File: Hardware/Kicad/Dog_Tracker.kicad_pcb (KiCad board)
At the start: 4 copper layers, 109 x 53.7 mm, 22 parts, among them IC1 M4 Feather, U1 ADP160AUJZ-1.8-R7, U2 SX1280IMLTRT, U3 Origin_GPS1510, U5 SN74AUP1T97, U6 LSM6DSO32

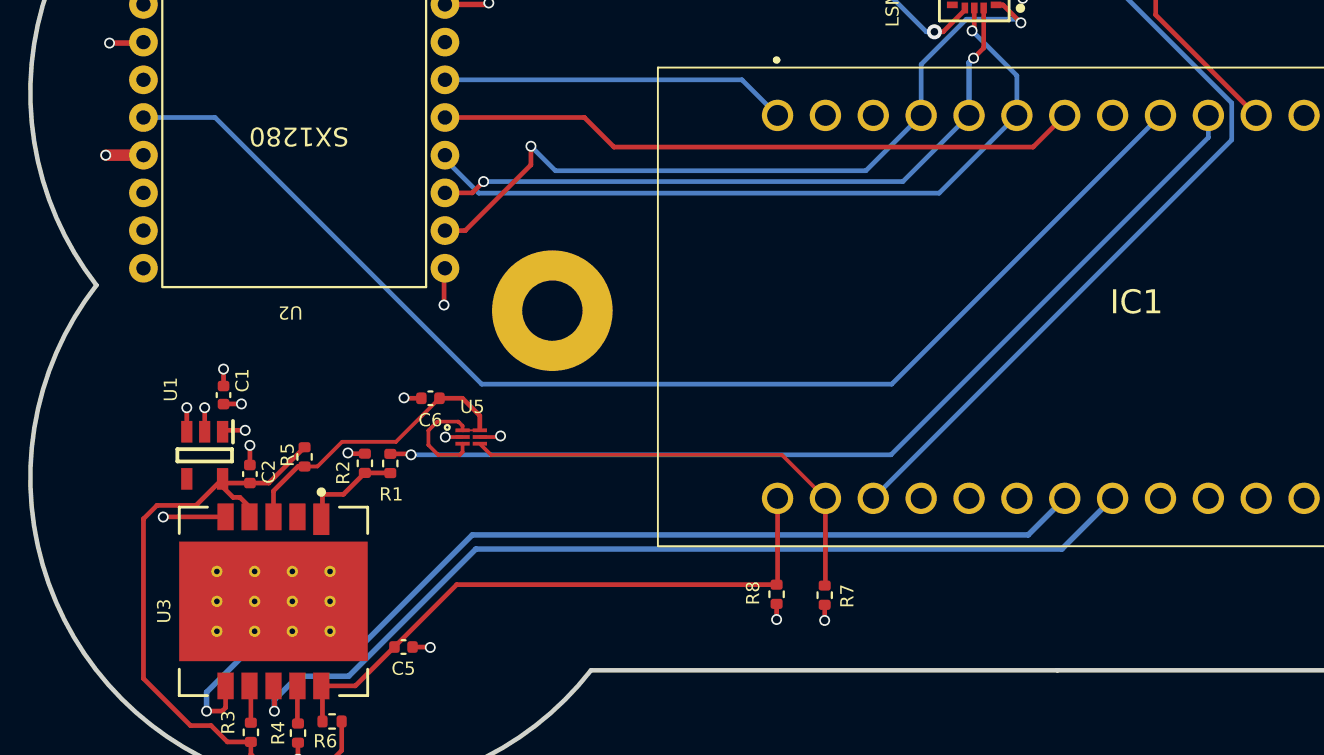
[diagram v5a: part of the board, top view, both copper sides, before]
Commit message: 'update pcb based on steves comments'
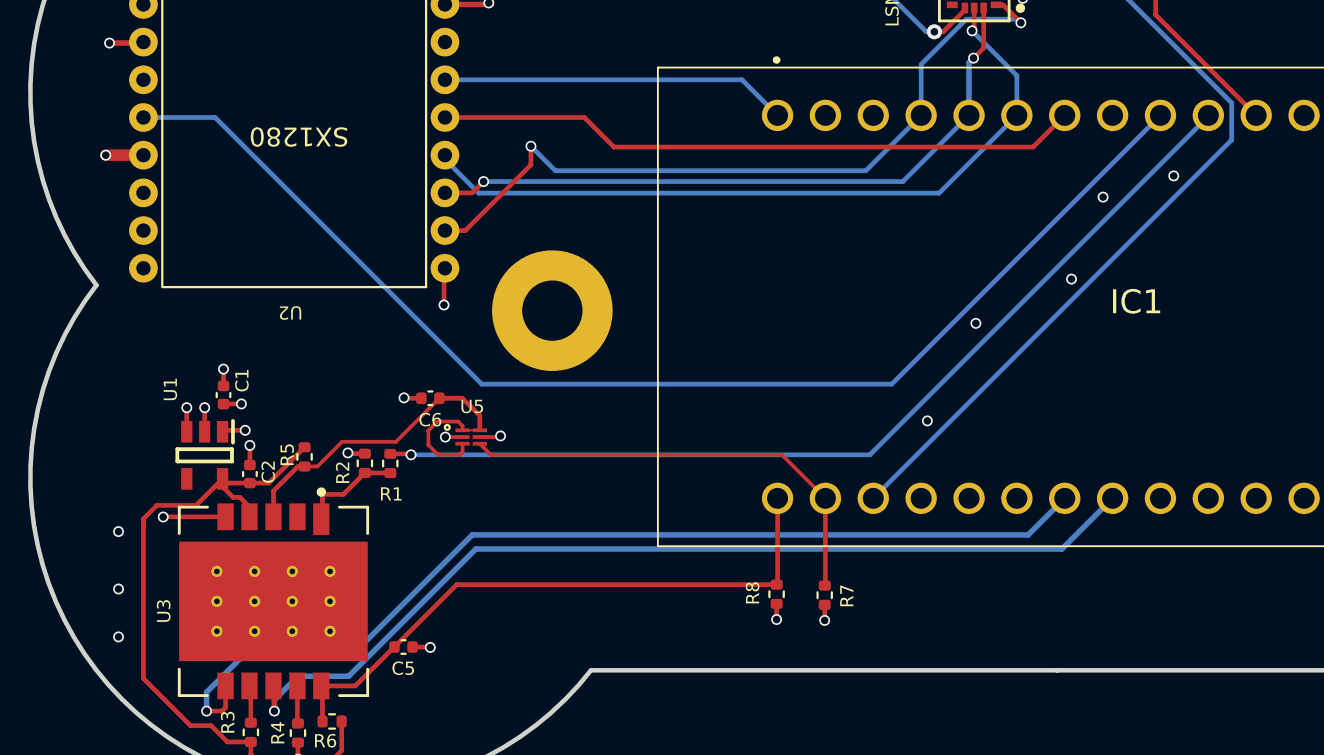
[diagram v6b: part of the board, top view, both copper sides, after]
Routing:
- net /GPS_ON: track 51.6 -> 50.9 mm
- net GND: vias 23 -> 31
- added copper zone on B.Cu, net GND
- added copper zone on F.Cu, net GND
- removed copper zone on F.Cu, net (none)
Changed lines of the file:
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@@
       (outputformat 1)
       (mirror false)
-      (drillshape 1)
+      (drillshape 0)
       (scaleselection 1)
-      (outputdirectory "")
+      (outputdirectory "./")
     )
   )
@@
   (segment (start 65.8 87.85) (end 63.55 87.85) (width 0.29337) (layer "F.Cu") (net 2))
   (via (at 58.4 111.65) (size 0.58) (drill 0.4) (layers "F.Cu" "B.Cu") (free) (net 2))
+  (via (at 96.8 102.425) (size 0.58) (drill 0.4) (layers "F.Cu" "B.Cu") (free) (net 2))
   (via (at 64.83 80.82) (size 0.8) (drill 0.4) (layers "F.Cu" "B.Cu") (net 2))
   (via (at 63.57 110.81) (size 0.58) (drill 0.4) (layers "F.Cu" "B.Cu") (net 2))
@@
   (via (at 94.2125 85.875) (size 0.58) (drill 0.4) (layers "F.Cu" "B.Cu") (free) (net 2))
   (via (at 45.75 89.9) (size 0.58) (drill 0.4) (layers "F.Cu" "B.Cu") (free) (net 2))
+  (via (at 98.475 98.075) (size 0.58) (drill 0.4) (layers "F.Cu" "B.Cu") (free) (net 2))
   (via (at 65.877798 87.772202) (size 0.58) (drill 0.4) (layers "F.Cu" "B.Cu") (free) (net 2))
   (via (at 64.83 78.82) (size 0.8) (drill 0.4) (layers "F.Cu" "B.Cu") (net 2))
   (via (at 51.8 107.2) (size 0.58) (drill 0.4) (layers "F.Cu" "B.Cu") (free) (net 2))
   (via (at 55.75 127.9) (size 0.58) (drill 0.4) (layers "F.Cu" "B.Cu") (free) (net 2))
+  (via (at 102.225 96.95) (size 0.58) (drill 0.4) (layers "F.Cu" "B.Cu") (free) (net 2))
+  (via (at 46.228 118.872) (size 0.58) (drill 0.4) (layers "F.Cu" "B.Cu") (free) (net 2))
   (via (at 91.3125 83.575) (size 0.58) (drill 0.4) (layers "F.Cu" "B.Cu") (free) (net 2))
   (via (at 48.6 115.05) (size 0.58) (drill 0.4) (layers "F.Cu" "B.Cu") (free) (net 2))
   (via (at 50.8 78.92) (size 0.8) (drill 0.4) (layers "F.Cu" "B.Cu") (net 2))
+  (via (at 89.15 109.95) (size 0.58) (drill 0.4) (layers "F.Cu" "B.Cu") (free) (net 2))
   (via (at 91.11 85.02) (size 0.58) (drill 0.4) (layers "F.Cu" "B.Cu") (free) (net 2))
   (via (at 53.2 111.25) (size 0.58) (drill 0.4) (layers "F.Cu" "B.Cu") (free) (net 2))
   (via (at 64.83 79.82) (size 0.8) (drill 0.4) (layers "F.Cu" "B.Cu") (net 2))
   (via (at 94.2125 87.525) (size 0.58) (drill 0.4) (layers "F.Cu" "B.Cu") (free) (net 2))
+  (via (at 46.228 121.412) (size 0.58) (drill 0.4) (layers "F.Cu" "B.Cu") (free) (net 2))
   (via (at 63.5 103.8) (size 0.58) (drill 0.4) (layers "F.Cu" "B.Cu") (free) (net 2))
+  (via (at 46.228 115.824) (size 0.58) (drill 0.4) (layers "F.Cu" "B.Cu") (free) (net 2))
   (via (at 89.2125 86.875) (size 0.58) (drill 0.4) (layers "F.Cu" "B.Cu") (free) (net 2))
   (via (at 50.8 109.25) (size 0.58) (drill 0.4) (layers "F.Cu" "B.Cu") (free) (net 2))
   (via (at 62.7715 121.973) (size 0.58) (drill 0.4) (layers "F.Cu" "B.Cu") (free) (net 2))
   (via (at 94.2125 86.725) (size 0.58) (drill 0.4) (layers "F.Cu" "B.Cu") (free) (net 2))
+  (via (at 91.725 104.775) (size 0.58) (drill 0.4) (layers "F.Cu" "B.Cu") (free) (net 2))
   (segment (start 52.007 126.987) (end 53.249999 126.987) (width 0.25) (layer "F.Cu") (net 3))
   (segment (start 56.99 128.52) (end 54.13 128.52) (width 0.25) (layer "F.Cu") (net 3))
@@
   (segment (start 61.7 111.7) (end 61.75 111.75) (width 0.25) (layer "F.Cu") (net 13))
   (via (at 61.75 111.75) (size 0.58) (drill 0.4) (layers "F.Cu" "B.Cu") (net 13))
-  (segment (start 61.75 111.75) (end 87.22 111.75) (width 0.25) (layer "B.Cu") (net 13))
-  (segment (start 87.22 111.75) (end 104.06 94.91) (width 0.25) (layer "B.Cu") (net 13))
-  (segment (start 104.06 94.91) (end 104.06 93.74) (width 0.25) (layer "B.Cu") (net 13))
+  (segment (start 104.06 93.79) (end 104.06 93.74) (width 0.25) (layer "B.Cu") (net 13))
+  (segment (start 61.75 111.75) (end 86.1 111.75) (width 0.25) (layer "B.Cu") (net 13))
+  (segment (start 86.1 111.75) (end 104.06 93.79) (width 0.25) (layer "B.Cu") (net 13))
   (segment (start 101.266 85.558) (end 101.266 88.406) (width 0.25) (layer "F.Cu") (net 14))
   (segment (start 101.266 88.406) (end 106.6 93.74) (width 0.25) (layer "F.Cu") (net 14))
@@
   (segment (start 55.719999 125.977) (end 55.749999 126.007) (width 0.25) (layer "F.Cu") (net 43))
   (segment (start 55.719999 124.012) (end 55.719999 125.977) (width 0.25) (layer "F.Cu") (net 43))
-  (zone (net 0) (net_name "") (layer "F.Cu") (hatch edge 0.508)
+  (zone (net 2) (net_name "GND") (layer "F.Cu") (hatch edge 0.508)
     (connect_pads (clearance 0))
     (min_thickness 0.254) (filled_areas_thickness no)
@@
     (polygon
       (pts
-        (xy 35.456116 143.032403)
-        (xy 36.9 68.05)
-        (xy 154.2 65.1)
-        (xy 154.5 137.15)
-        (xy 35.456116 143.032403)
         (xy 35.451267 143.284178)
         (xy 35.1 143.05)
+        (xy 35.456116 143.032403)
       )
     )
@@
         (xy 63.28 86.07)
         (xy 52.48 86.07)
+      )
+    )
+  )
+  (zone (net 0) (net_name "") (layer "F.Cu") (hatch edge 0.508)
+    (connect_pads (clearance 0))
+    (min_thickness 0.254)
+    (keepout (tracks allowed) (vias allowed) (pads allowed ) (copperpour not_allowed) (footprints allowed))
+    (fill (thermal_gap 0.508) (thermal_bridge_width 0.508))
+    (polygon
+      (pts
+        (xy 60.594 125.568)
+        (xy 48.375 125.575)
+        (xy 47.6 125)
+        (xy 47.05 124.15)
+        (xy 47.052 113.717)
+        (xy 60.594 113.717)
+      )
+    )
+  )
+  (zone (net 2) (net_name "GND") (layer "F.Cu") (hatch edge 0.508)
+    (connect_pads (clearance 0))
+    (min_thickness 0.254) (filled_areas_thickness no)
+    (fill yes (thermal_gap 0.508) (thermal_bridge_width 0.508))
+    (polygon
+      (pts
+        (xy 154.2 65.1)
+        (xy 154.5 137.15)
+        (xy 35.456116 143.032403)
+        (xy 36.9 68.05)
       )
     )
@@
     )
   )
-  (zone (net 0) (net_name "") (layer "B.Cu") (hatch edge 0.508)
+  (zone (net 2) (net_name "GND") (layer "B.Cu") (hatch edge 0.508)
     (connect_pads (clearance 0))
     (min_thickness 0.254) (filled_areas_thickness no)

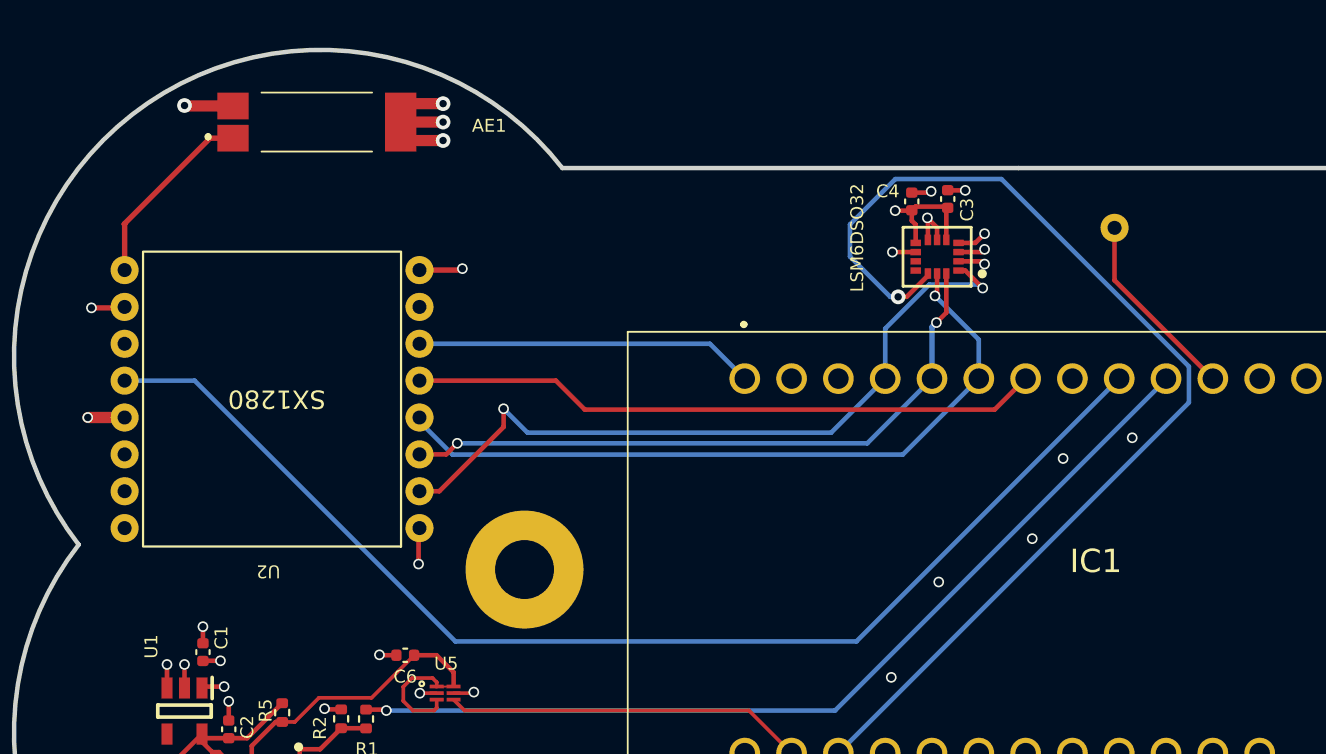
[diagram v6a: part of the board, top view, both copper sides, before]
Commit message: fixed footprint
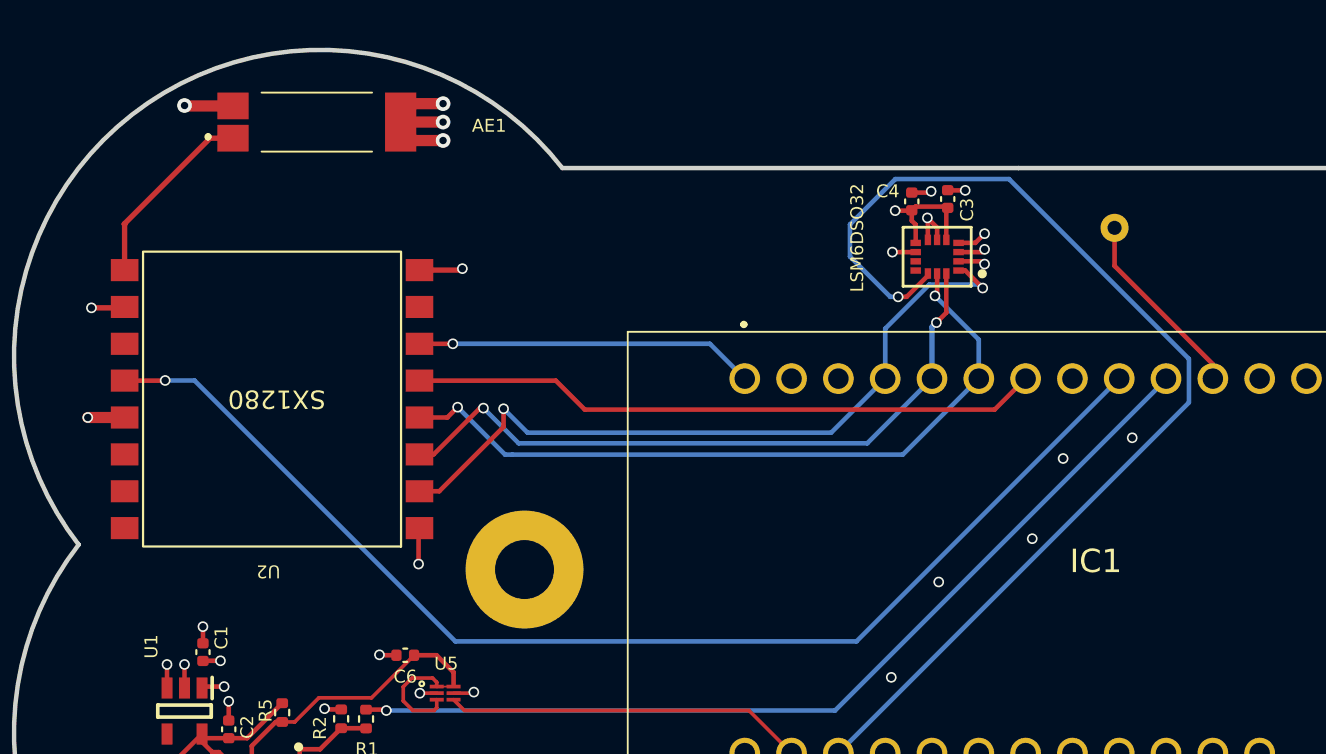
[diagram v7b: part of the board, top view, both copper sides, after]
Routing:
- net /MOSI: track 35.5 -> 37.1 mm
- net /SCK: track 39.8 -> 40.1 mm, vias 1 -> 2
- net /BUSY: vias 0 -> 1
- net /lora reset: vias 0 -> 1

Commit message: 'add vias'
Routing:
- net GND: vias 31 -> 63
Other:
- board size 109 x 53.7 mm -> 100 x 53.9 mm
